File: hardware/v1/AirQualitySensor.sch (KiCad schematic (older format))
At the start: 44 parts, among them J1 USB_C_Receptacle_USB2.0, J2 SWD, J3 UART, U1 004-0-0053, U2 DHT22, U3 XC6206P332MR

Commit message: Fix ferrite bead having wrong footprint
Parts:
- FB1, FB2: footprint Inductor_SMD:L_0603_1608Metric -> Inductor_SMD:L_0805_2012Metric
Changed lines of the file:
@@
 F 0 "FB2" V 2613 1500 50  0000 C CNN
 F 1 "100R" V 2704 1500 50  0000 C CNN
-F 2 "Inductor_SMD:L_0603_1608Metric" V 2780 1500 50  0001 C CNN
+F 2 "Inductor_SMD:L_0805_2012Metric" V 2780 1500 50  0001 C CNN
 F 3 "~" H 2850 1500 50  0001 C CNN
 F 4 "GZ2012D101TF" H 2850 1500 50  0001 C CNN "Description"
@@
 F 0 "FB1" V 2613 1050 50  0000 C CNN
 F 1 "100R" V 2704 1050 50  0000 C CNN
-F 2 "Inductor_SMD:L_0603_1608Metric" V 2780 1050 50  0001 C CNN
+F 2 "Inductor_SMD:L_0805_2012Metric" V 2780 1050 50  0001 C CNN
 F 3 "~" H 2850 1050 50  0001 C CNN
 F 4 "GZ2012D101TF" H 2850 1050 50  0001 C CNN "Description"

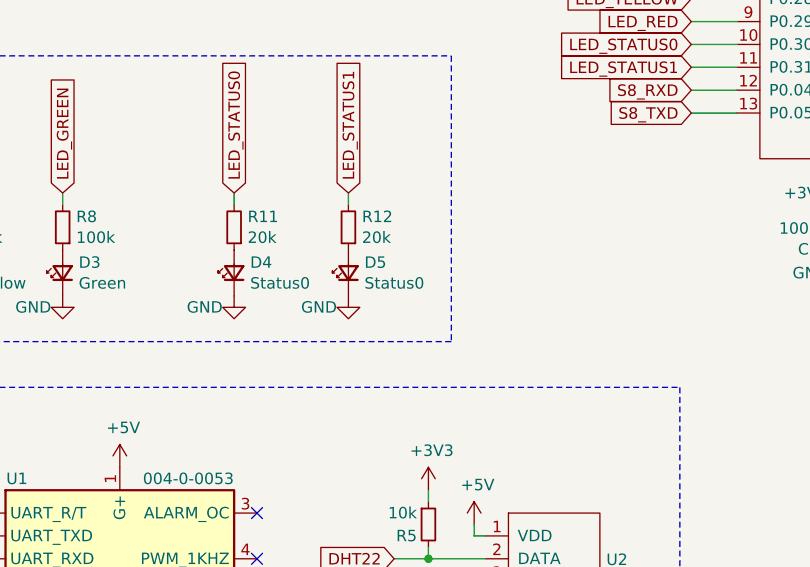
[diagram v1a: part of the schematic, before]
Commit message: Fix Status1 LED typo
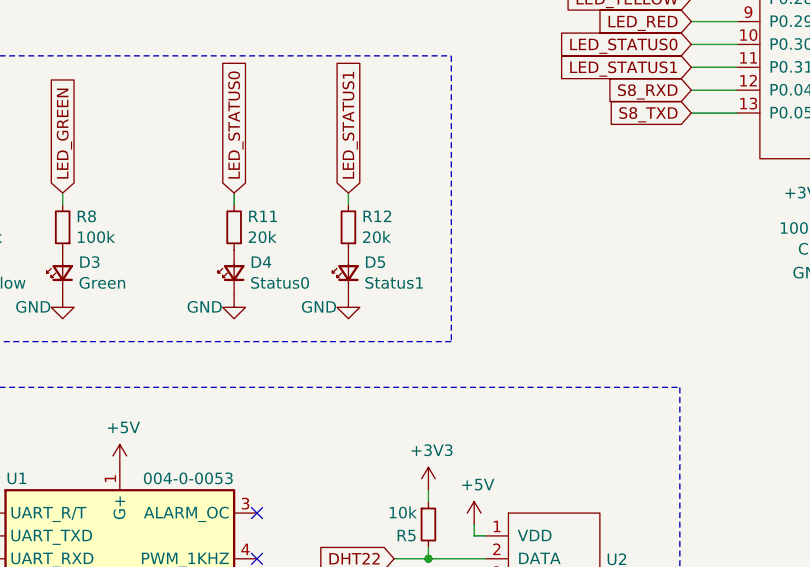
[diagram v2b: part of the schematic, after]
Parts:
- D5: value Status0 -> Status1
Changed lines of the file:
@@
 P 3200 5600
 F 0 "D5" V 3246 5530 50  0000 R CNN
-F 1 "Status0" V 3155 5530 50  0000 R CNN
+F 1 "Status1" V 3155 5530 50  0000 R CNN
 F 2 "LED_SMD:LED_0805_2012Metric" V 3200 5600 50  0001 C CNN
 F 3 "~" V 3200 5600 50  0001 C CNN
